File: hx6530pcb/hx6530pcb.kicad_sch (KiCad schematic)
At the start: 10 parts, among them SW1 SW_Push, U1 PIC16F73-ISO

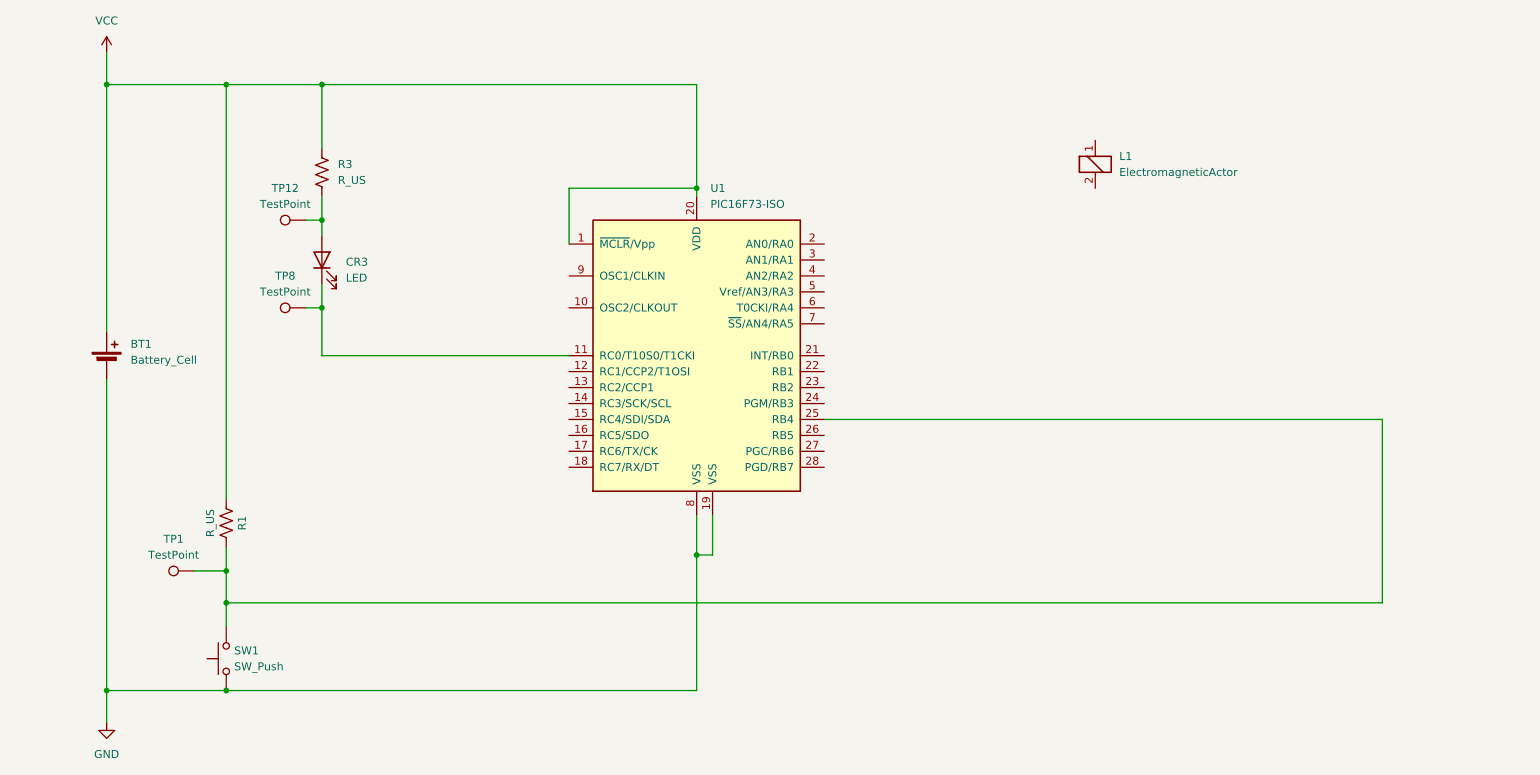
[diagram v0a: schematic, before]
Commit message: Coil and MOSFETs
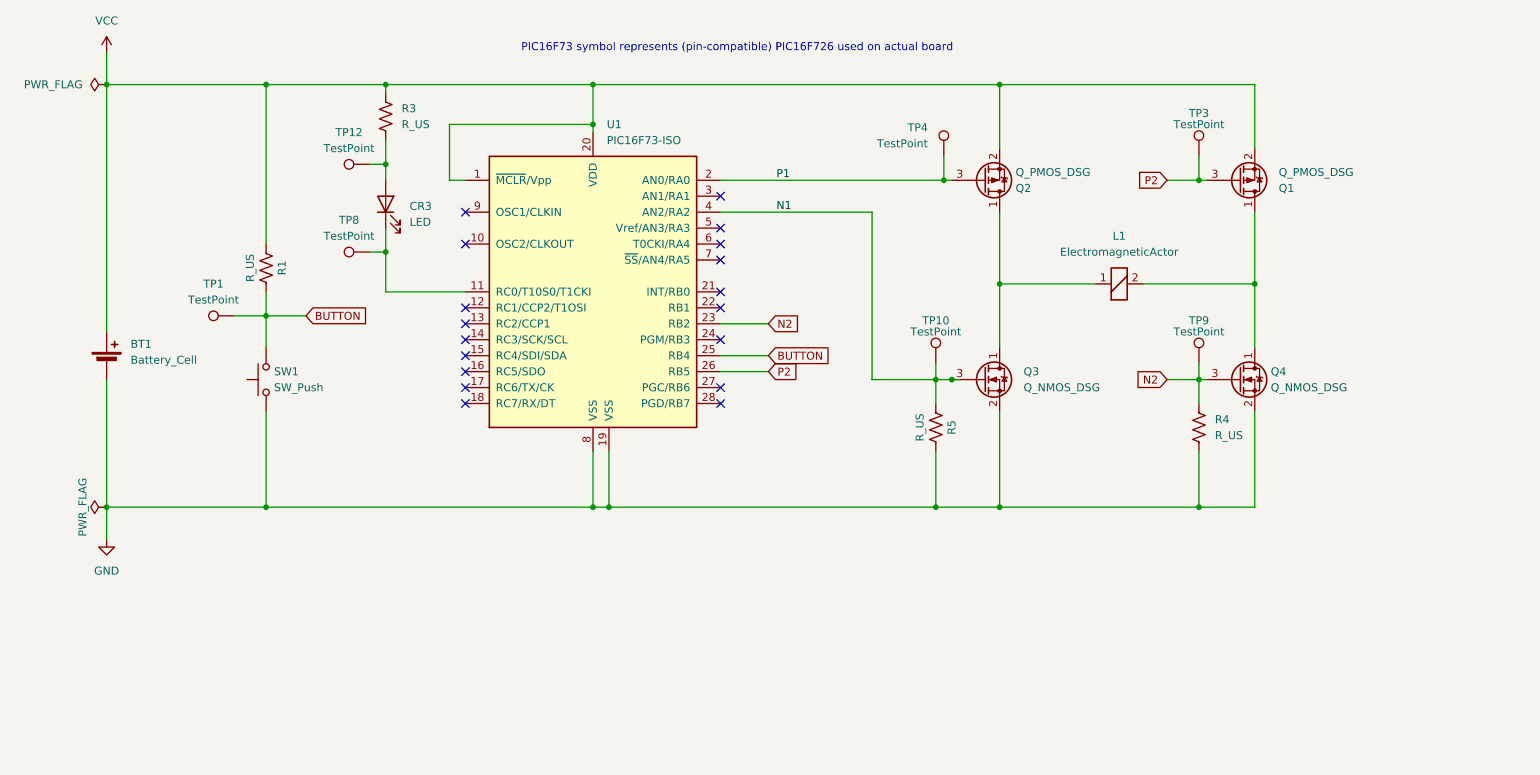
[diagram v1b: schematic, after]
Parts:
- added Q1, Q2: Q_PMOS_DSG, symbol Device:Q_PMOS_DSG
- added Q3, Q4: Q_NMOS_DSG, symbol Device:Q_NMOS_DSG
- added R4, R5: R_US, symbol Device:R_US
- added TP10, TP3, TP4, TP9: TestPoint, symbol Connector:TestPoint
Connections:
- net GND: now also Q3.2 (S), Q4.2 (S), R4.2, R5.2
- net VCC: now also Q1.2 (S), Q2.2 (S)
- net BUTTON: now reaches R1.2, SW1.2, TP1.1, U1.25 (RB4)
- net at L1.1 (-): now also Q2.1 (D), Q3.1 (D)
- net at L1.2 (+): now also Q1.1 (D), Q4.1 (D)
- net P1: now reaches U1.2 (AN0/RA0)
- net P1: now also Q2.3 (G), TP4.1
- net N2: now reaches U1.23 (RB2)
- net N2: now also Q4.3 (G), R4.1, TP9.1
- net P2: now reaches U1.26 (RB5)
- net P2: now also Q1.3 (G), TP3.1
- net N1: now reaches U1.4 (AN2/RA2)
- net N1: now also Q3.3 (G), R5.1, TP10.1
- no-connect marks 0 -> 18
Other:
- note added: "PIC16F73 symbol represents (pin-compatible) PIC16F726 used on actual board"
- moved on the sheet: CR3, L1, R1, R3, SW1, TP1, TP12, TP8, U1

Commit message: Polyfuse, decoupling cap, resistor values
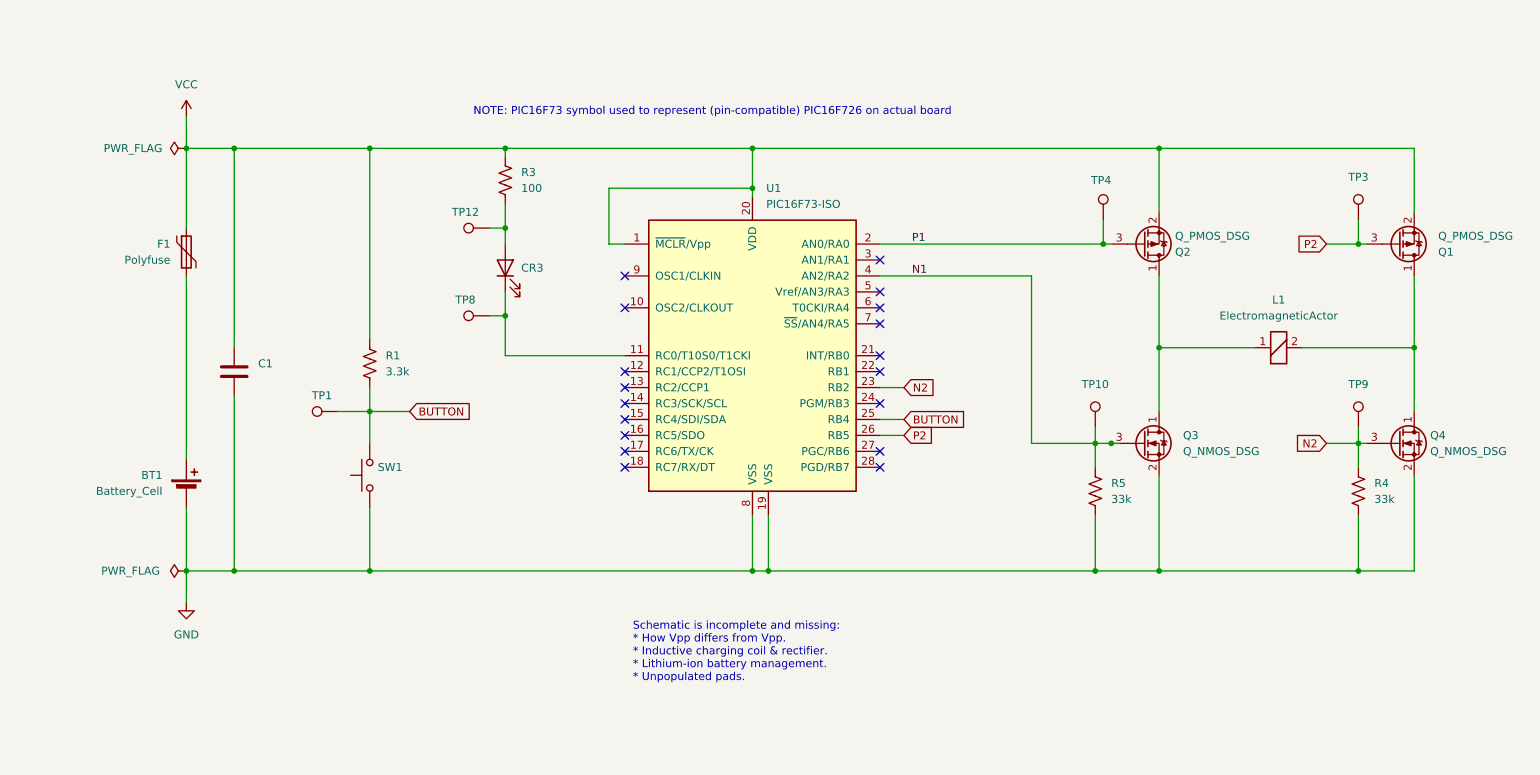
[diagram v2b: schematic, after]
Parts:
- added C1: C, symbol Device:C
- added F1: Polyfuse, symbol Device:Polyfuse
- R1: value R_US -> 3.3k
- R3: value R_US -> 100
- R4, R5: value R_US -> 33k
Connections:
- net GND: now also C1.2
- net VCC: now also C1.1, F1.1; no longer BT1.1 (+)
- new net: BT1.1 (+), F1.2
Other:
- note added: "NOTE: PIC16F73 symbol used to represent (pin-compatible) PIC16F726 on actual board"
- note added: "Schematic is incomplete and missing: * How Vpp differs from Vpp. * Inductive charging coil & rectifier. * Lithium-ion battery management. * Unpopulated pads."
- note removed: "PIC16F73 symbol represents (pin-compatible) PIC16F726 used on actual board"
- moved on the sheet: BT1, CR3, L1, Q1, Q2, Q3, Q4, R1, R3, R4, R5, SW1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

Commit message: Reminder this is highly suspect
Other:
- note added: "Drain/Source doesn't make sense Do I have something backwards?"
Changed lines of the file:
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@@
+    (effects (font (size 1.27 1.27)) (justify left bottom))
+  )
+  (text "Drain/Source doesn't make sense\nDo I have something backwards?"
+    (at 205.74 149.86 0)
     (effects (font (size 1.27 1.27)) (justify left bottom))
   )
